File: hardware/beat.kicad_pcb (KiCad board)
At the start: 4 copper layers, 60 x 35 mm, 67 parts, among them J101 Cortex_Debug, J102 DX07S016JA3, J103 1x08, J601 SJ2-25404B-SMT-TR, Q201 IQE006NE2LM5CG, Q301 IQE006NE2LM5CG, Q401 IQE006NE2LM5CG, Q501 IQE006NE2LM5CG, SW101 SKSG, SW102 SKSG, U101 TPS78433QWDRBRQ1, U102 ATSAMD51G, U601 TLP2361, U701 TPS2559, Y101 32k768

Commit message: Replace Order_Number
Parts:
- H101, H102, H103, H104: value MountingHole_2mm -> 2mm
- INFO102: value Order_Number -> ~; footprint V2_Production:Order_Number -> V2_Production:Revision
- J101: value Cortex_Debug -> Cortex

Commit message: Update Library
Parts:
- C110: value 22u -> 10u
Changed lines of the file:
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@@
 		)
 		(group ""
-			(members "24cf1cd4-0364-49b3-9db9-9453fc00a4b5" "36105c46-a4de-4349-9497-7058f14c10ed"
-				"6b34a744-3736-4996-8007-c14286f0c616" "8140d242-111b-4cef-a899-37b4fb2d9b96"
-				"8a7c8d3c-2f39-48cf-b662-d66beec52218" "c237cbac-c637-400d-8b29-48cd6bc06411"
+			(members "2e40ee80-f471-4ee4-bc99-48316354225d" "426ba025-29c5-4f4d-8167-35850534bad0"
+				"4cc068d9-df55-45fd-8fba-45ab29935858" "7a176a1b-a4b3-4bd8-865a-15e1cd8184e2"
+				"df639a1e-5be1-4be5-89ea-746220664464" "f9eb72f1-6fc6-49da-82d3-6f1c421930bf"
 			)
 		)
 		(group ""
-			(members "41557350-160e-4be9-b2b8-12abe6962eb5" "4d3d3198-2df6-444b-aee1-0e67c39660a9"
-				"660fbfa3-34a8-4a4c-81a7-ea54e76bf779" "a27d10a3-5998-4abf-8899-e02b4e755bba"
-				"a4f02e3d-e287-4c41-8dfb-dd5a08f72fd7" "e48ab2bd-a1fc-44ab-9169-3bd77cb0a510"
+			(members "6cc2f6b9-6f6e-4289-bbc4-f5683d4555d0" "86a7bac0-e3a0-4d5a-9f4d-5afdacc0b4d5"
+				"93ec5cfa-0937-499b-9a5e-7c0143f09f32" "b2507a74-88a7-48e7-a162-ee390945754d"
+				"c946d612-f519-4b1c-9e01-b3fc9485d5a6" "f4d62df5-c121-470d-b9a7-fae2f0fb3bac"
 			)
 		)
@@
 			)
 		)
-		(property "Value" "22u"
+		(property "Value" "10u"
 			(at 0 2.3 0)
 			(layer "F.Fab")

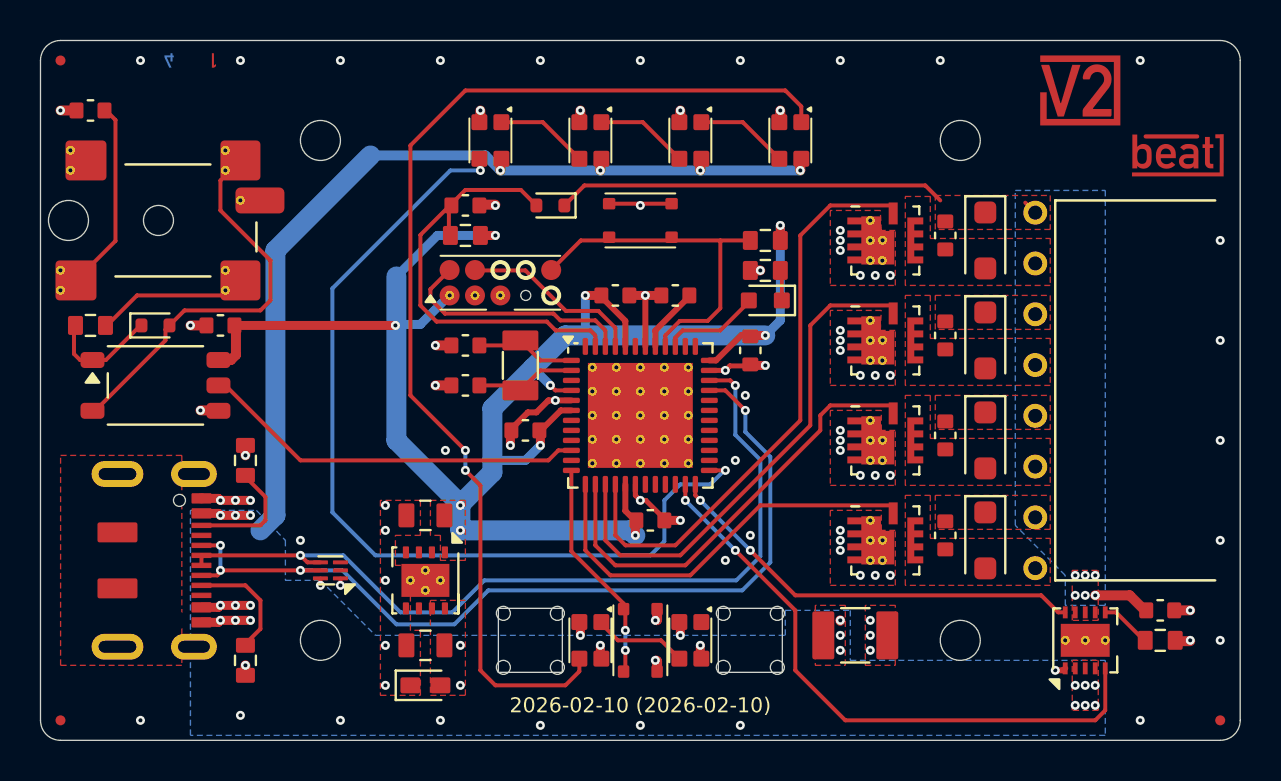
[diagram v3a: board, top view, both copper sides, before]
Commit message: Replace diode
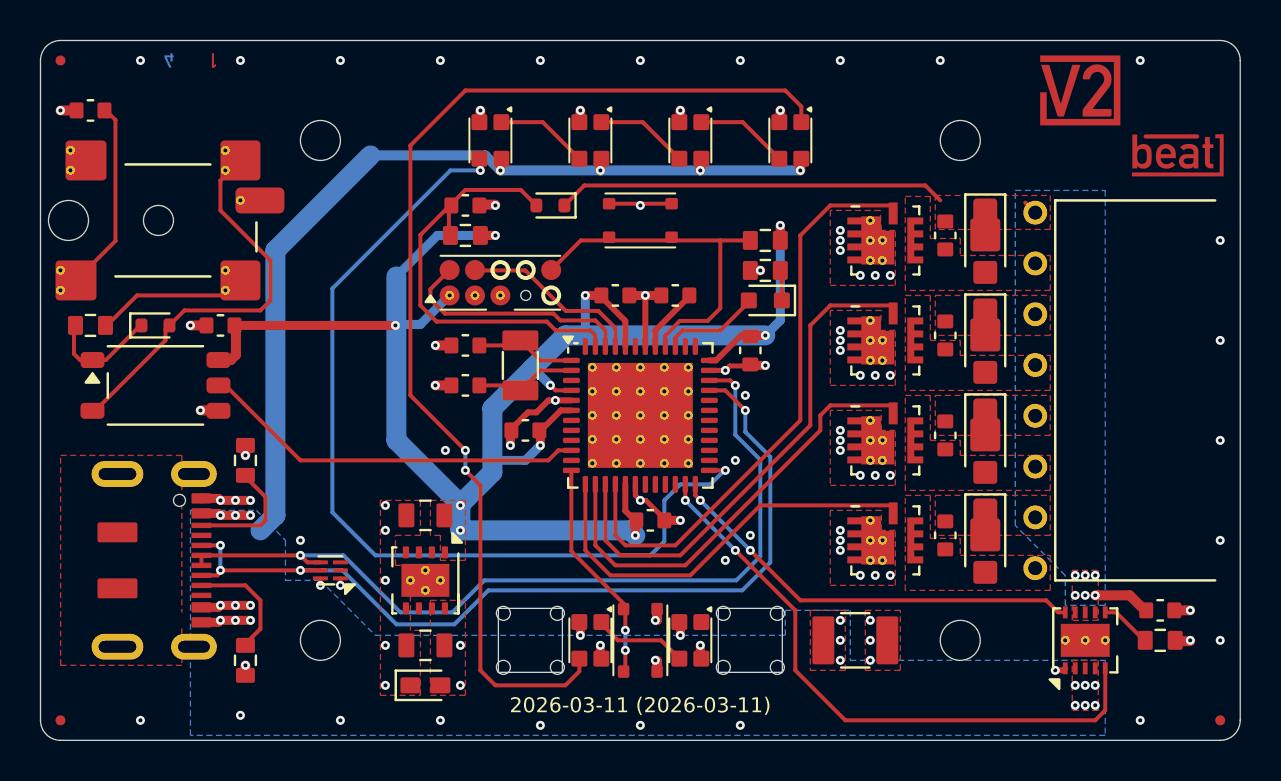
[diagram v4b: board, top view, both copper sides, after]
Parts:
- C110: value 10u -> 22u
- D201, D301, D401, D501: value S310FA -> PMEG6030AEXEX; footprint V2_Diode_SMD:D_SOD-123F -> V2_Diode_SMD:D_SOD-123HP
- moved C110 0.25 mm to (157.8, 110.0)

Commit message: Update ESD suppressor
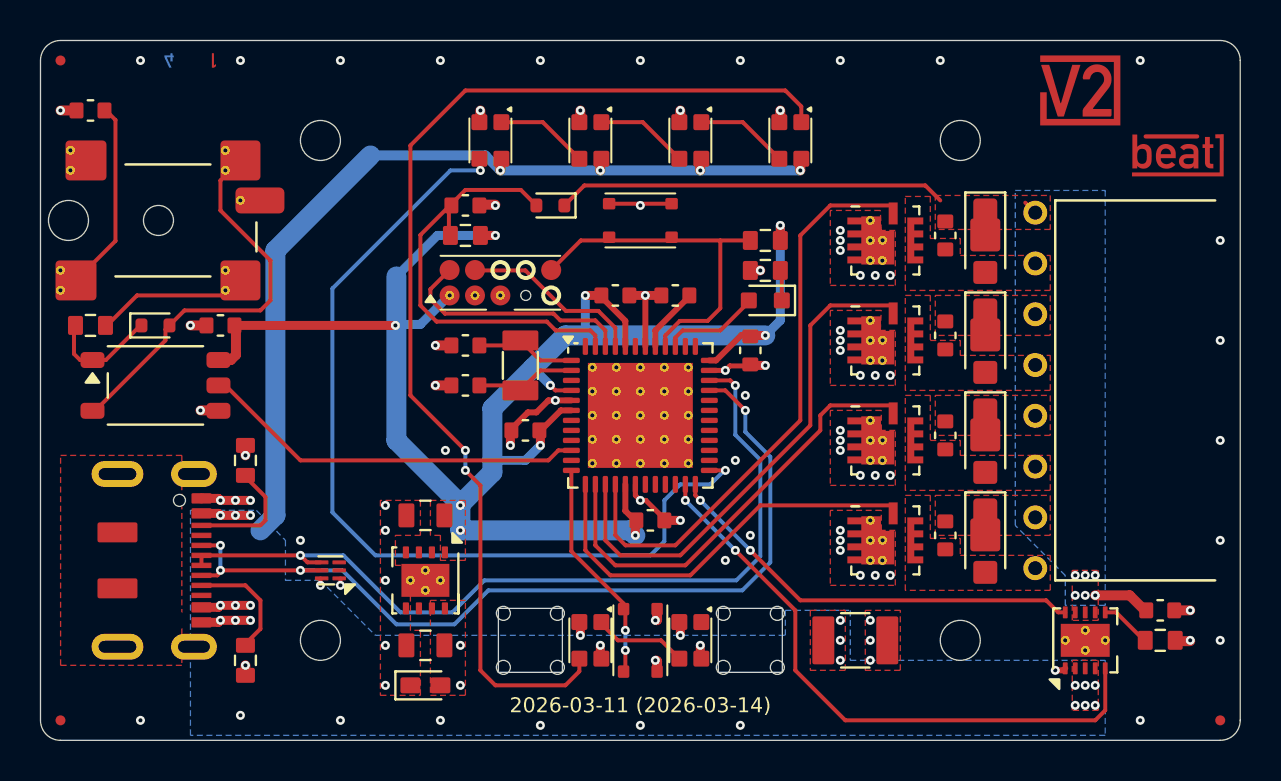
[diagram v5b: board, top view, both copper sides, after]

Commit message: Replace diode
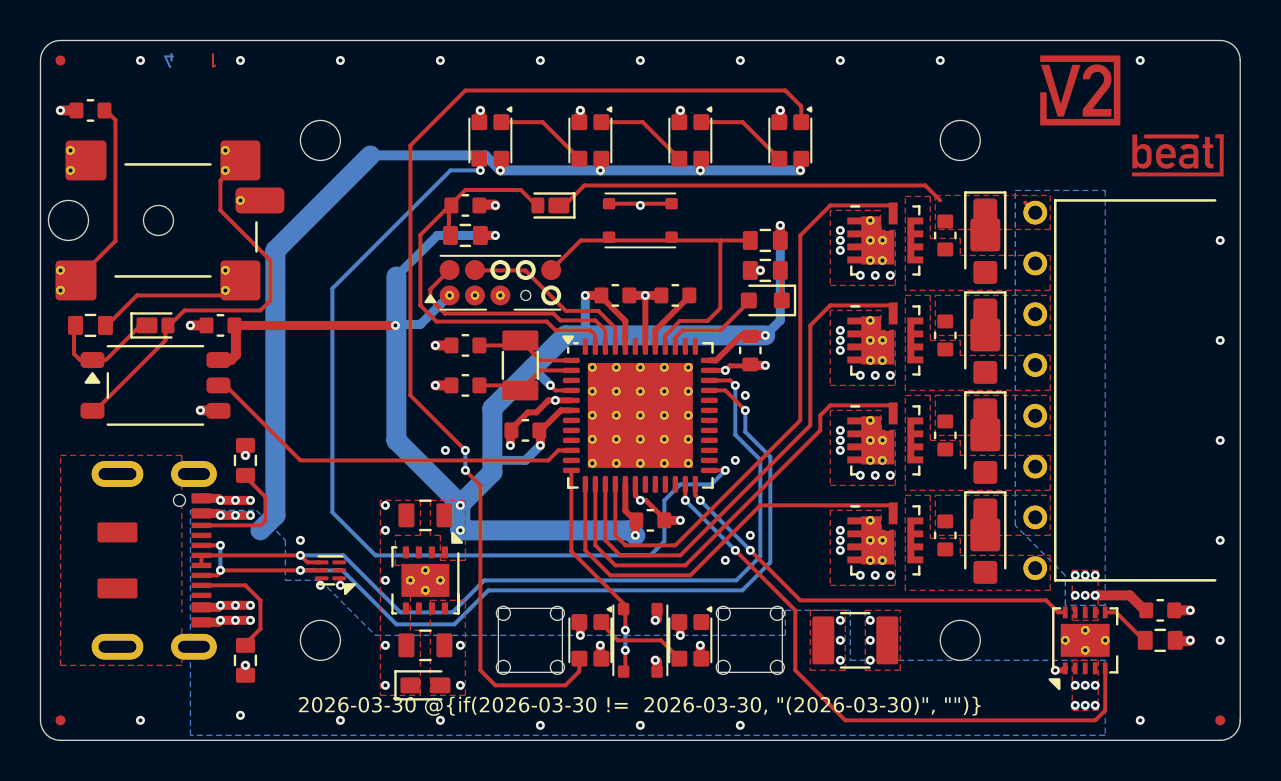
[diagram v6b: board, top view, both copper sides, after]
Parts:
- D104, D601: value RB501SM -> PMEG2010EPK; footprint V2_Diode_SMD:D_SOD-523 -> V2_Diode_SMD:D_SOD-1608
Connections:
- net Shield renamed /Shield

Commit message: Update
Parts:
- renumbered C108 to C101, C109 to C102, C101 to C103, C102 to C104, C103 to C105, C104 to C106, C105 to C107, C112 to C108, C111 to C109, C106 to C110, C107 to C111, C110 to C112, C602 to C601, C601 to C602, D104 to D101, D103 to D102, D101 to D103, D102 to D104, ICON102 to ICON101, ICON101 to ICON102, INFO102 to INFO101, INFO101 to INFO102, J103 to J102, J102 to J103, R104 to R101, R105 to R102, R101 to R103, R102 to R104, R103 to R105, SW102 to SW101, SW101 to SW102, U102 to U101, U101 to U102
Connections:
- net /VDDCORE renamed /+VCORE
